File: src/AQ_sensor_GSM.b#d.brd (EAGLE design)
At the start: 110.2 x 66.3 mm, 161 parts, among them J1 F-1X03-SIP-100-32, J2 53261-0871, J3 PJ-002BH, J4 S8411-45R, Q2 MMBT2222, Q3 MMBT2222, Q4 MMBT2222, Q5 MMBT2222, Q6 MMBT2222, Q7 MMBT2222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

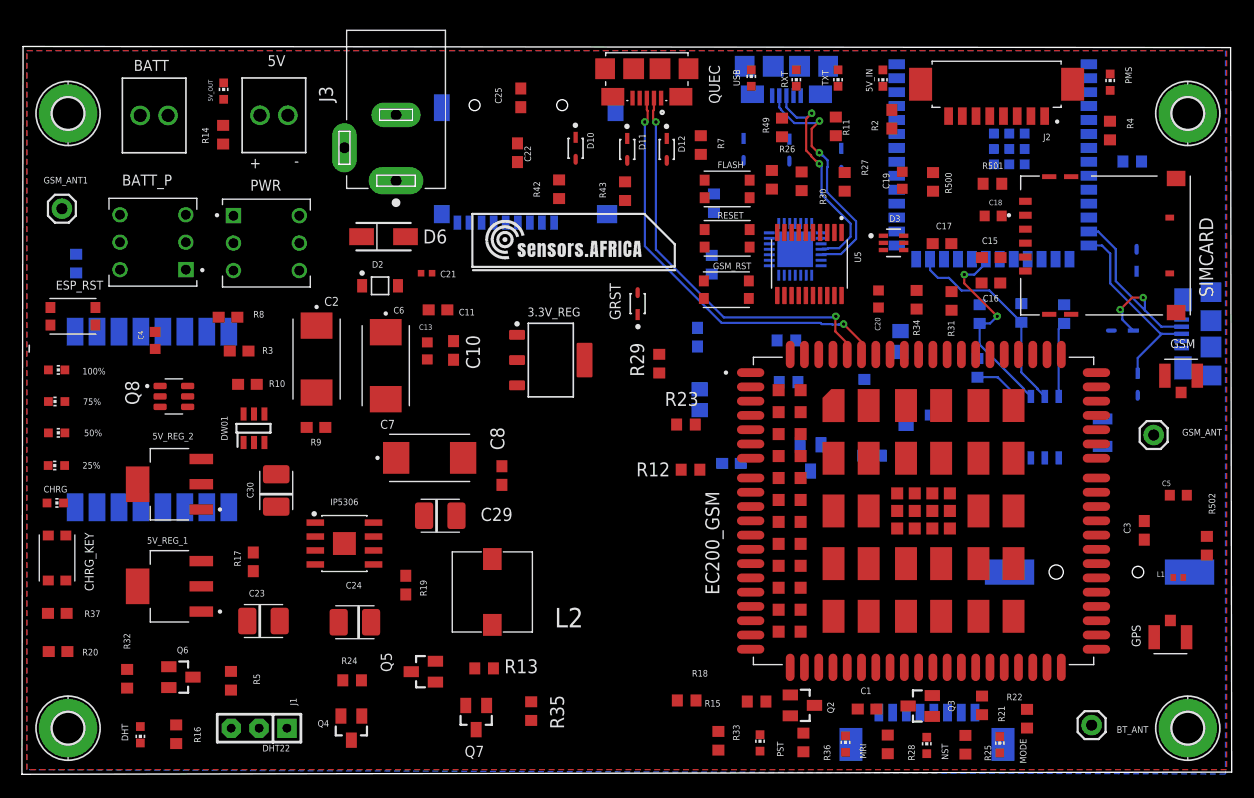
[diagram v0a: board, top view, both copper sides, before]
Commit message: Differential Pair routing
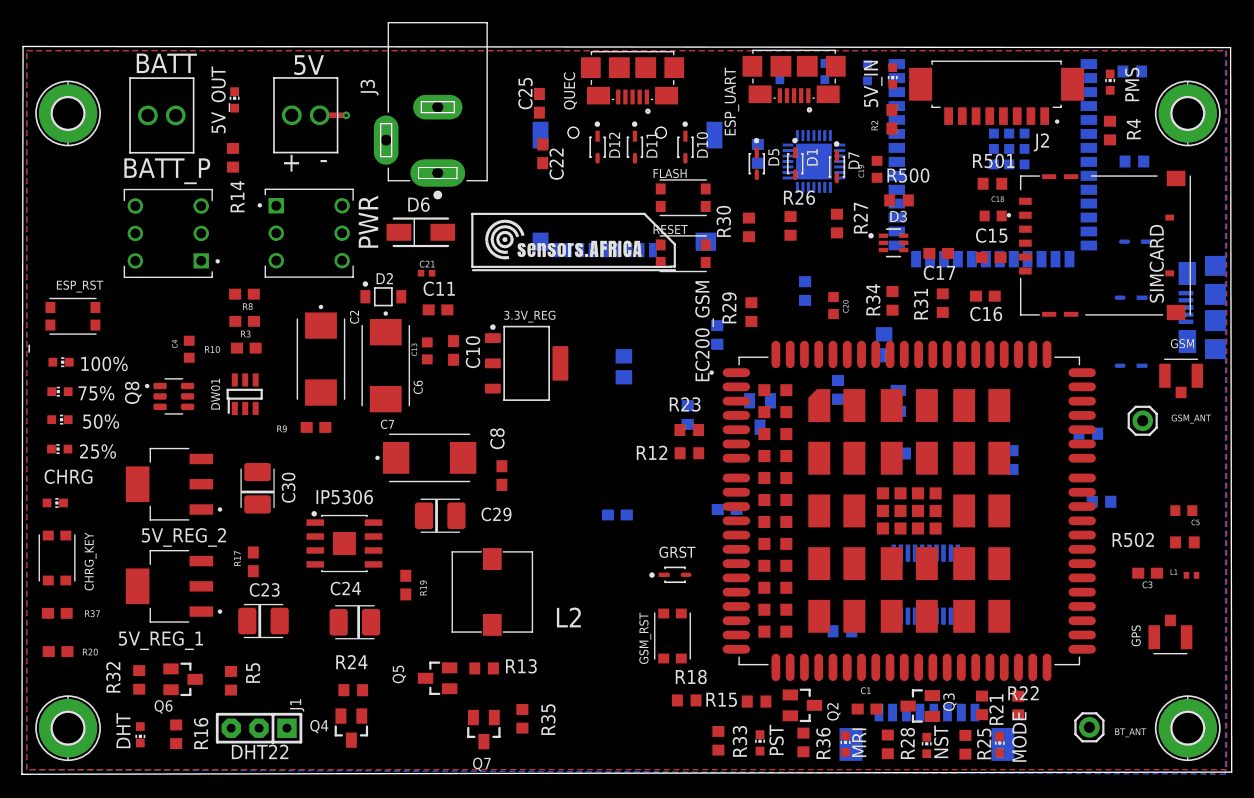
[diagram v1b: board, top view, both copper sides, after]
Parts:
- removed GSM_ANT1: (no value), SparkFun-Connectors:1X01
- removed J4: S8411-45R, S8411-45R:HARWIN_S8411-45R
- removed R41, R6: 0R, rcl:R0603
- removed R44, R45, R50: 47K, rcl:R0603
- removed U$1: SX1278, sx1278S2:SX1278
- removed U2: DS1307Z, SparkFun-Clocks:SO08-0.15
- removed Y1: 32.768kHz, SparkFun-Clocks:CRYSTAL-SMD-3.2X1.5MM
- moved R42 53.1 mm to (97.2, 30.5), flipped to the bottom, turned to 0 degrees
- moved R11 41.9 mm to (98.4, 24.3), flipped to the bottom, turned to 0 degrees
- moved R7 39.9 mm to (101.2, 63.5), flipped to the bottom, turned to 0 degrees
- moved R49 36.9 mm to (90.3, 28.1), flipped to the bottom, turned to 90 degrees
- moved R48 35.5 mm to (74.8, 12.5), turned to 0 degrees
- moved GSM_RST 31.9 mm to (59.3, 12.1), turned to 270 degrees
- moved U5 31.1 mm to (82.4, 16.8), flipped to the bottom
- moved GRST 24.9 mm to (59.6, 17.7), turned to 0 degrees
- moved R43 21.2 mm to (60.7, 32.2), flipped to the bottom
- moved C33 17.8 mm to (54.3, 23.1), turned to 0 degrees
- moved D10 10.0 mm to (60.5, 56.6)
- moved R29 9.63 mm to (66.5, 41.6)
- moved MICRO_SD1 9.34 mm to (55.3, 54.4)
- moved D7 8.65 mm to (74.3, 54.8), flipped to the top
- moved R1 8.43 mm to (71.4, 43.5), turned to 270 degrees
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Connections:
- net EUART_N renamed EUART_D-
- net EUART_P renamed EUART_D+
- net G_USB_N renamed G_USB_D-
- net G_USB_P renamed G_USB_D+
- net MCU_RXD renamed MCU-RXD_N
- net MCU_TXD renamed MCU-TXD_P
- removed net L_MIS0: U$1.13, X1.38
- removed net L_MOSI: U$1.14, X1.39
- removed net L_NRESET: U$1.4, X1.24
- removed net L_NSS: U$1.15, X1.16
- removed net L_SCK: U$1.12, X1.15
- removed net N$35: R6.2, U$1.1
- removed net N$50: U2.1, Y1.P$2
- removed net N$51: U2.2, Y1.P$1
- removed net N$58: J4.P, U2.3
- removed net N$59: J4.N, U2.4
- removed net N$6: GSM_ANT1.1, R6.1
- removed net N$63: R41.1, U2.8
- removed net RTC_SCL: R45.2, U2.6, X1.21
- removed net RTC_SDA: R50.2, U2.5, X1.20
- removed net RTC_SQW: R44.2, U2.7, X1.25
- new net +5V: C33.2, C34.2, R46.1, U1.7
- new net EUSB_D+: ESP_USB.3, X1.14
- new net EUSB_D-: X1.13
- new net IO1: X1.39
- new net IO12: X1.20
- new net IO13: X1.21
- new net IO2: X1.38
- new net IO3: X1.15
- new net IO46: X1.16
- new net IO47: X1.24
- new net IO48: X1.25
- net +3V3: no longer U$1.3
- net 5V_OUT: no longer C33.2, C34.2, R41.2, R44.1, R45.1, R46.1, R50.1, U1.7
- net EUSB_N: no longer X1.13
- net EUSB_P: no longer ESP_USB.3, X1.14
- net GND: no longer U$1.16, U$1.2, U$1.9
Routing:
- net G_USB_D+: track 38.3 -> 0.00 mm, vias 2 -> 0
- net G_USB_D-: track 37.0 -> 0.00 mm, vias 2 -> 0
- net EUART_D-: track 21.9 -> 0.00 mm, vias 2 -> 0
- net EUART_D+: track 20.1 -> 0.00 mm, vias 2 -> 0
- net EUSB_N: track 19.9 -> 0.00 mm, vias 2 -> 0
- net RTC_SQW: track 18.9 -> 0.00 mm
- net RTC_SCL: track 18.3 -> 0.00 mm, vias 2 -> 0
- net EUSB_P: track 17.9 -> 0.00 mm
- net N$63: track 6.86 -> 0.00 mm
- net RTC_SDA: track 4.32 -> 0.00 mm
- net GND: track 0.00 -> 2.42 mm, vias 0 -> 1
